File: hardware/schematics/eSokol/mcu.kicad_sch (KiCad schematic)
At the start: 24 parts, among them J1 DB25, J2 MOT_DRV_THR, Q10 AO3400A, Q11 BC547, Q12 AO3400A, Q6 AO3400A, Q9 AO3400A, SW1 SW_KEY, U2 YAAJ_BluePill_SWD_Breakout, U3 TP4056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

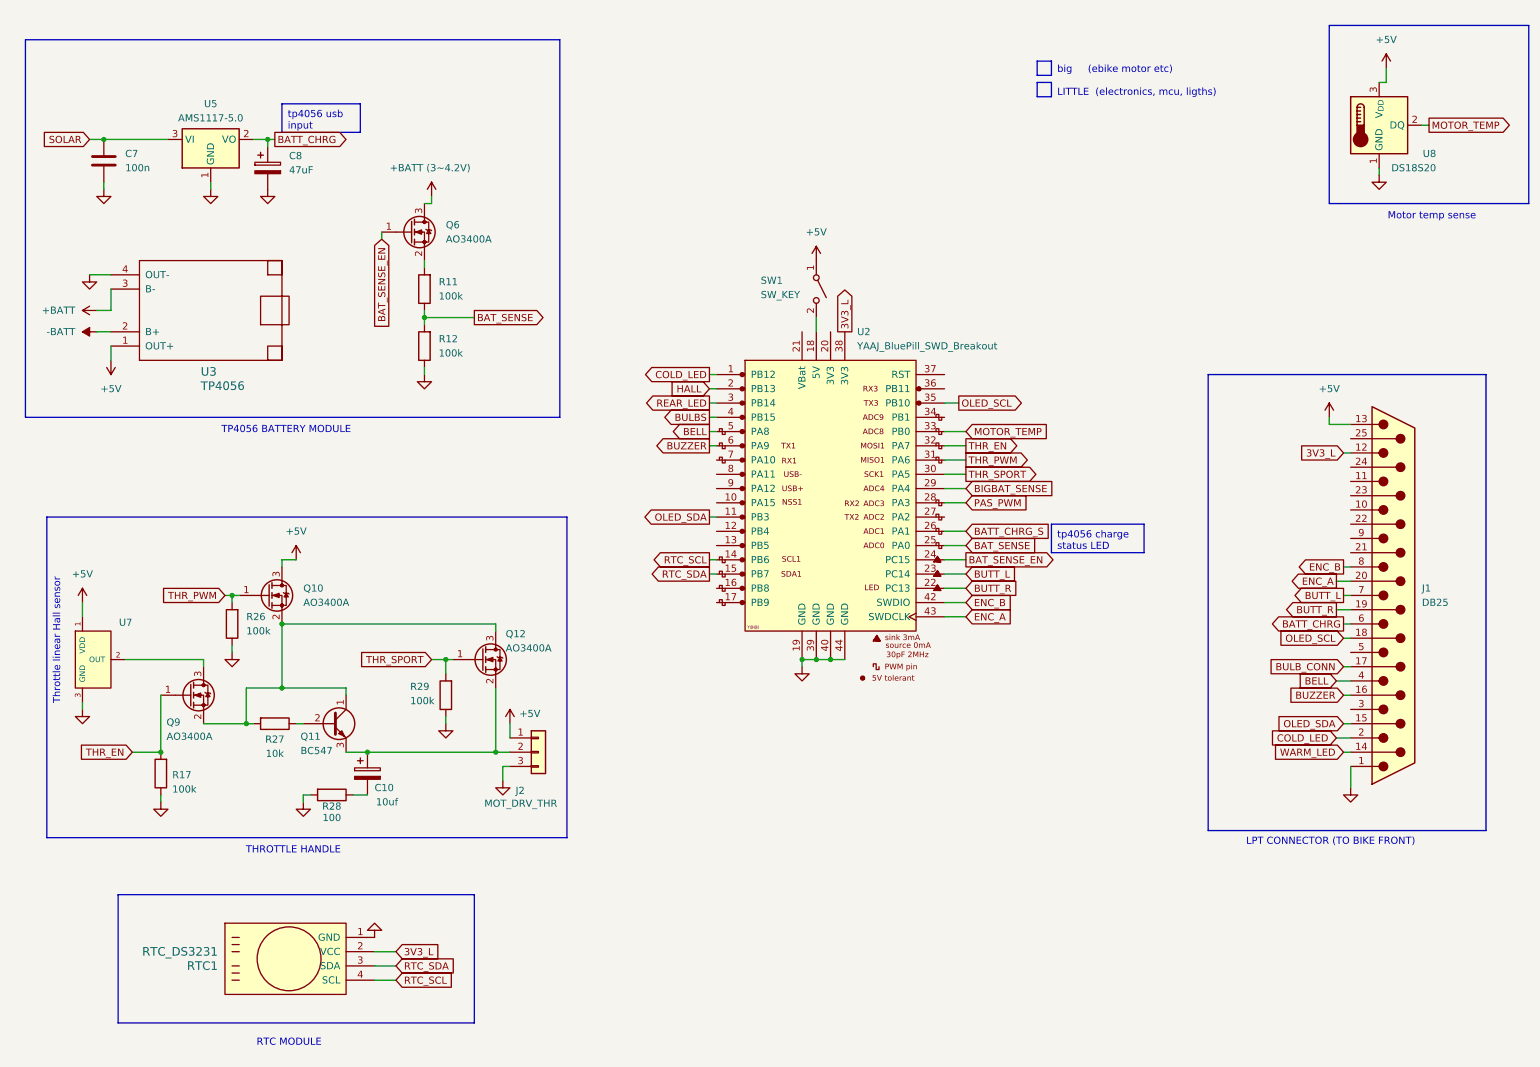
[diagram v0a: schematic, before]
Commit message: hardware: schematics: Fix improper NMOS placement, misc minor fixes
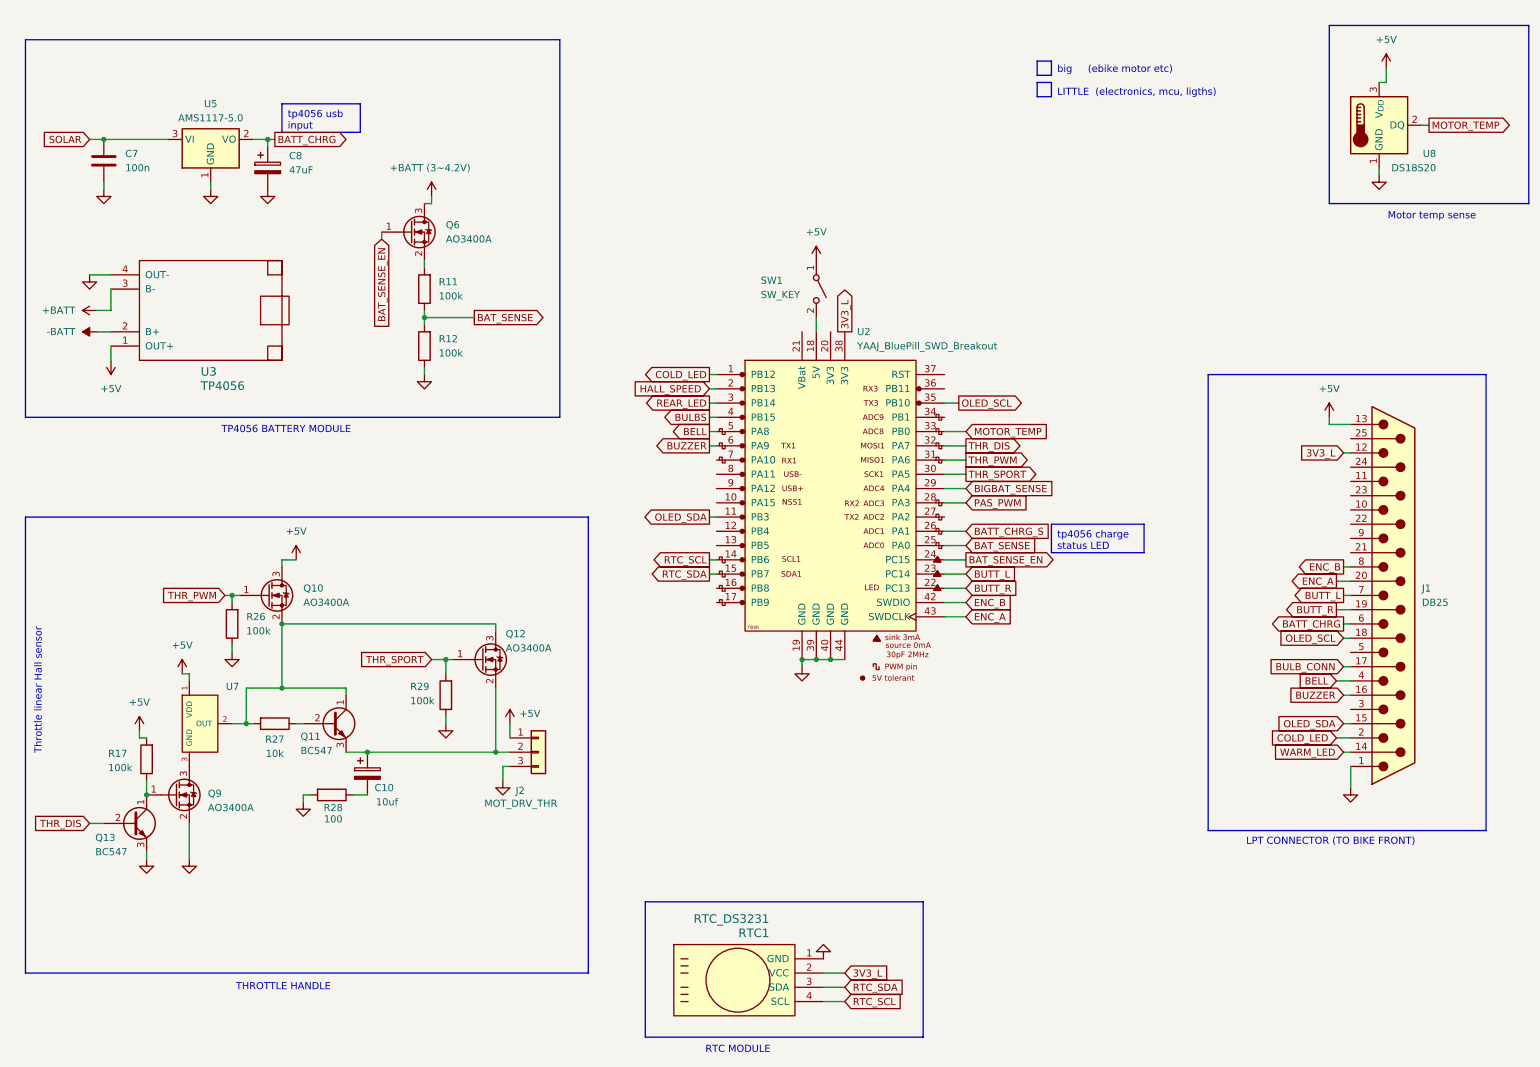
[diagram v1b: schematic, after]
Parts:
- added Q13: BC547, Package_TO_SOT_THT:TO-92_Inline, symbol Transistor_BJT:BC547
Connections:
- net +5V: now also R17.2
- net GND: now also Q9.2 (S), Q13.3 (E); no longer R17.1, U7.3 (GND)
- net at Q10.2 (S), Q11.1 (C), Q12.3 (D)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: now also U7.2 (OUT); no longer Q9.2 (S)
- net at Q9.3 (D): now also U7.3 (GND); no longer U7.2 (OUT)
- net HALL renamed HALL_SPEED
- removed net THR_EN: Q9.1 (G), R17.2, U2.32 (PA7)
- new net: Q13.1 (C), Q9.1 (G), R17.1
- new net THR_DIS: Q13.2 (B), U2.32 (PA7)
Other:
- moved on the sheet: R17, RTC1, U7

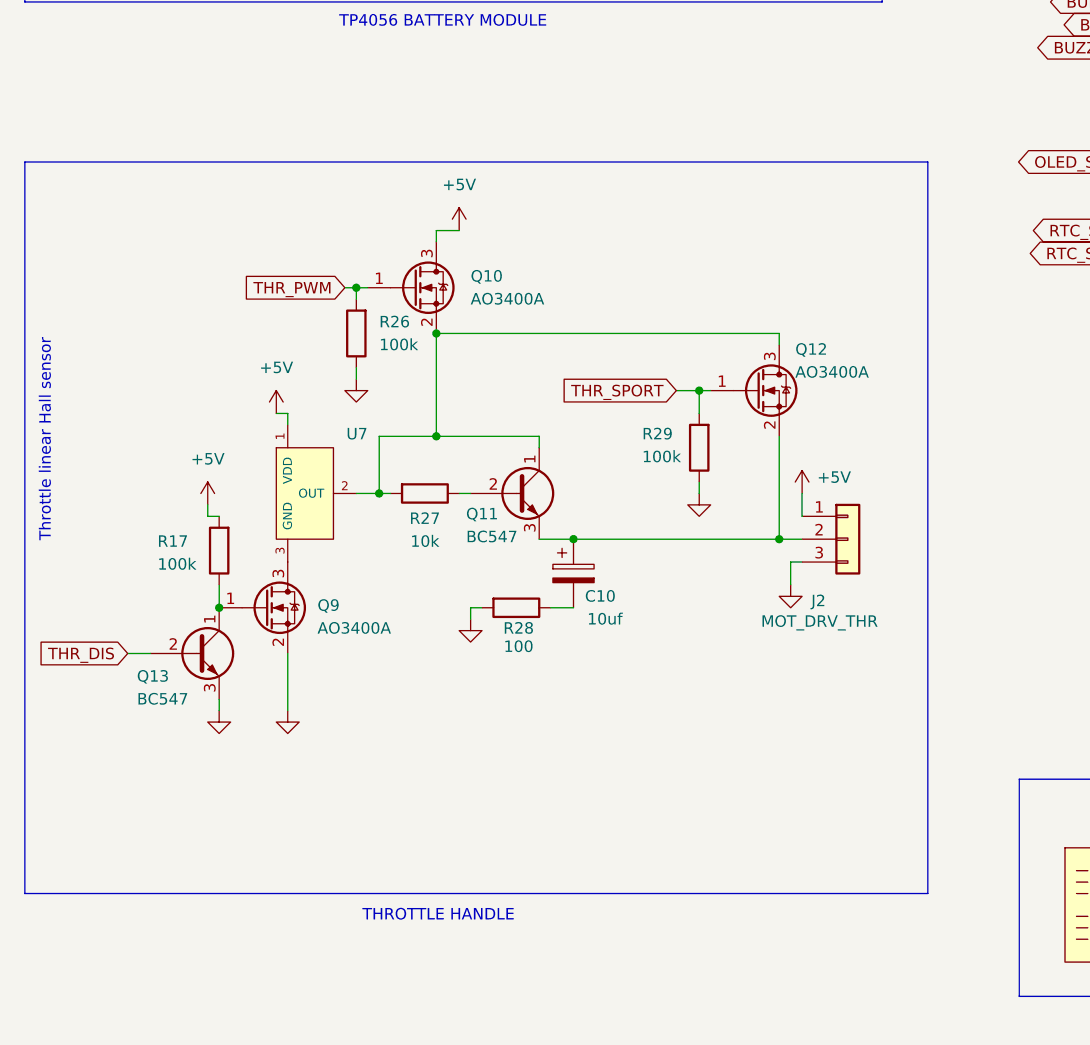
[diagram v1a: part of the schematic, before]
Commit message: Fix throttle transistor layout once more, move throttle to a separate page. Still needs testing.
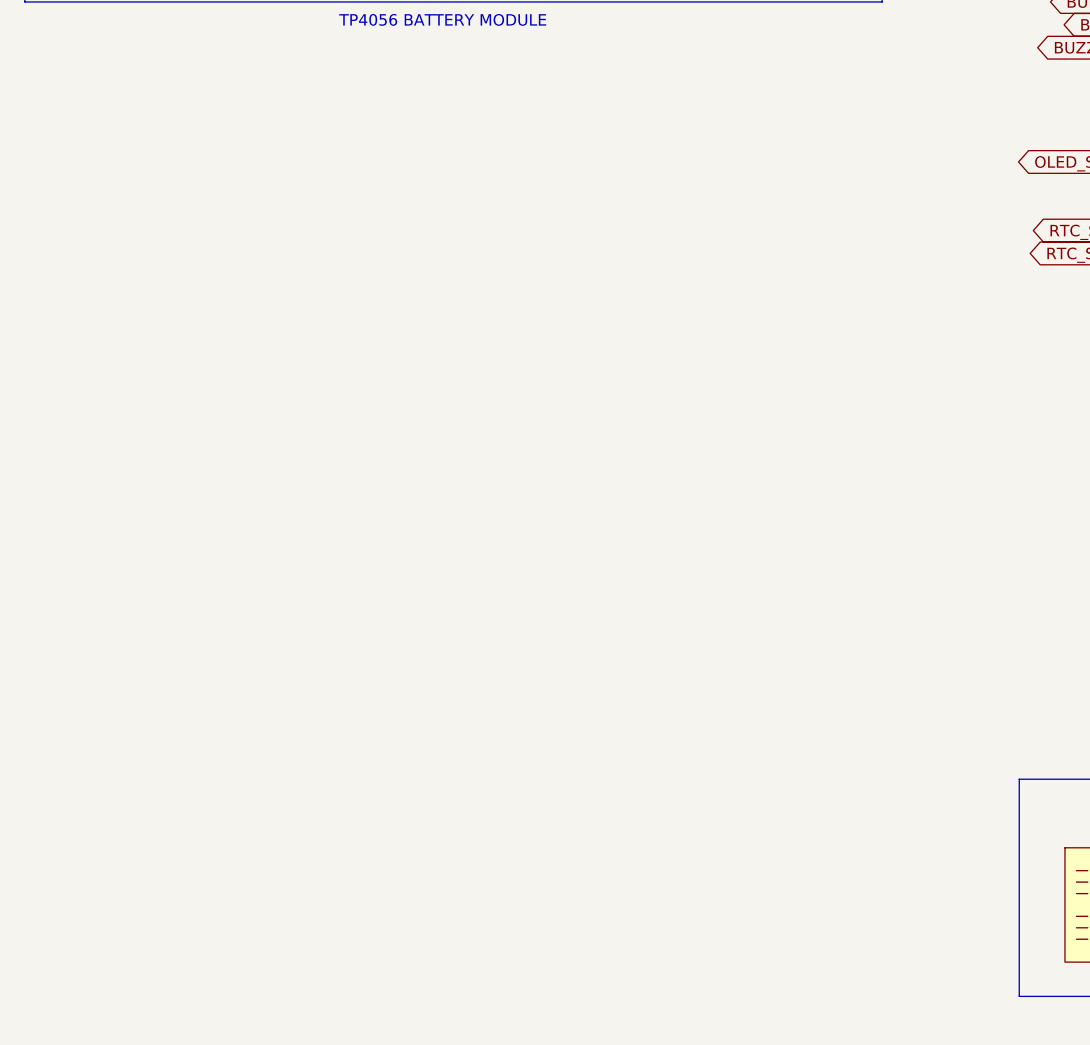
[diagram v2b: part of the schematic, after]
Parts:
- removed C10: 10uf, symbol Device:C_Polarized
- removed J2: MOT_DRV_THR, symbol Connector_Generic:Conn_01x03
- removed Q10, Q12, Q9: AO3400A, Package_TO_SOT_SMD:SOT-23, symbol Transistor_FET:AO3400A
- removed Q11, Q13: BC547, Package_TO_SOT_THT:TO-92_Inline, symbol Transistor_BJT:BC547
- removed R17, R26, R29: 100k, symbol Device:R
- removed R27: 10k, symbol Device:R
- removed R28: 100, symbol Device:R
- removed U7: Hall_Sensor, Package_TO_SOT_SMD:SOT-23, symbol 49e:Hall_Sensor
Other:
- note removed: "THROTTLE HANDLE"
- note removed: "Throttle linear Hall sensor"

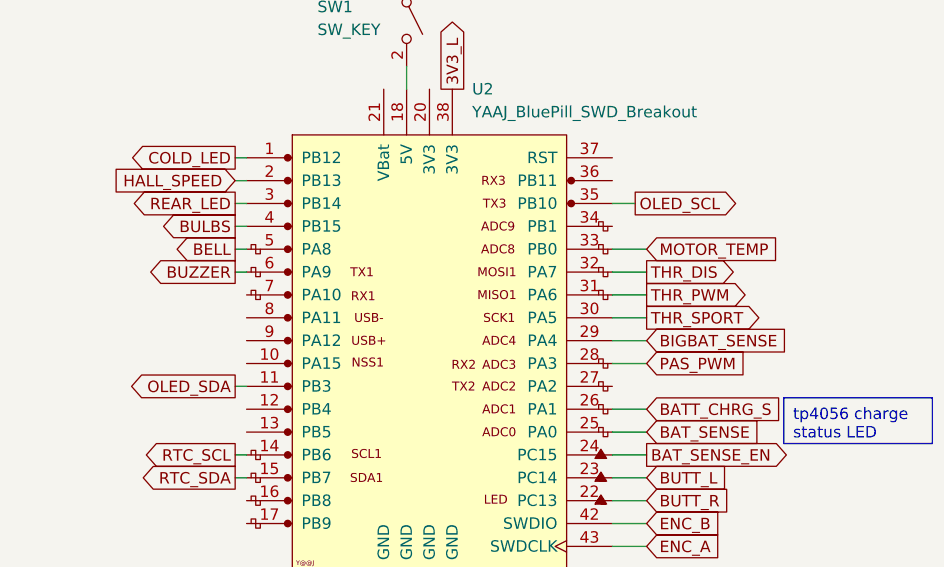
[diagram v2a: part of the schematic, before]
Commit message: schematics: (almost) finalize throttle circuit (it's working :D), minor cleanups
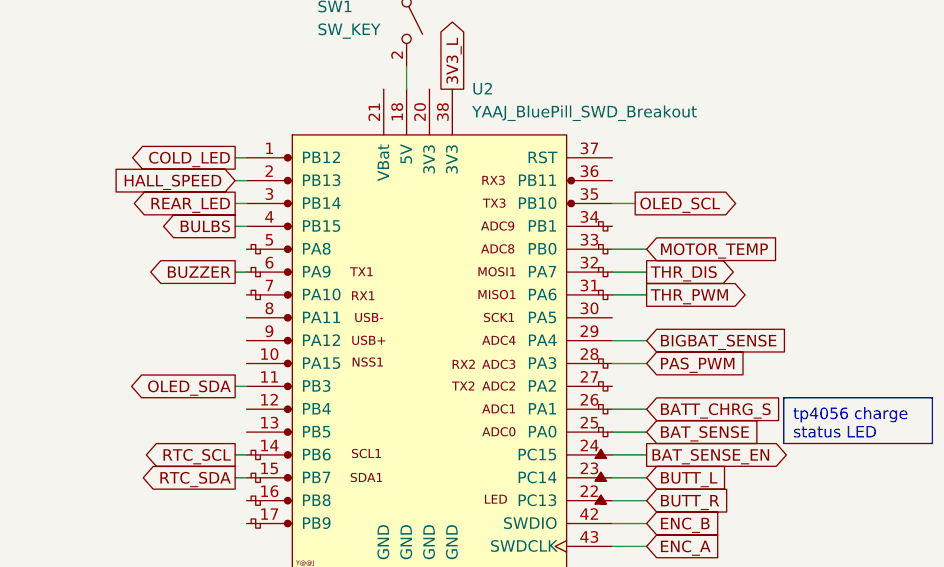
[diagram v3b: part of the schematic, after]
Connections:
- net BELL: no longer U2.5 (PA8)
- net THR_SPORT: no longer names the net of U2.30 (PA5)
